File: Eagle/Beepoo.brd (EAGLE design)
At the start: 100 x 80 mm, 66 parts, among them CN1 JACK4PTH, CN2 SD-MICRO, CN3 USB-MC5F01, J1 JUMPER3-1.5MM, J2 JUMPER3-1.5MM, SW2 SLIDE1-PCM12, U1 RT9266-SOT23, U2 ATMEGA32U4, U3 AY-3-8912/28, U4 OPAMP-DUAL-SOIC8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

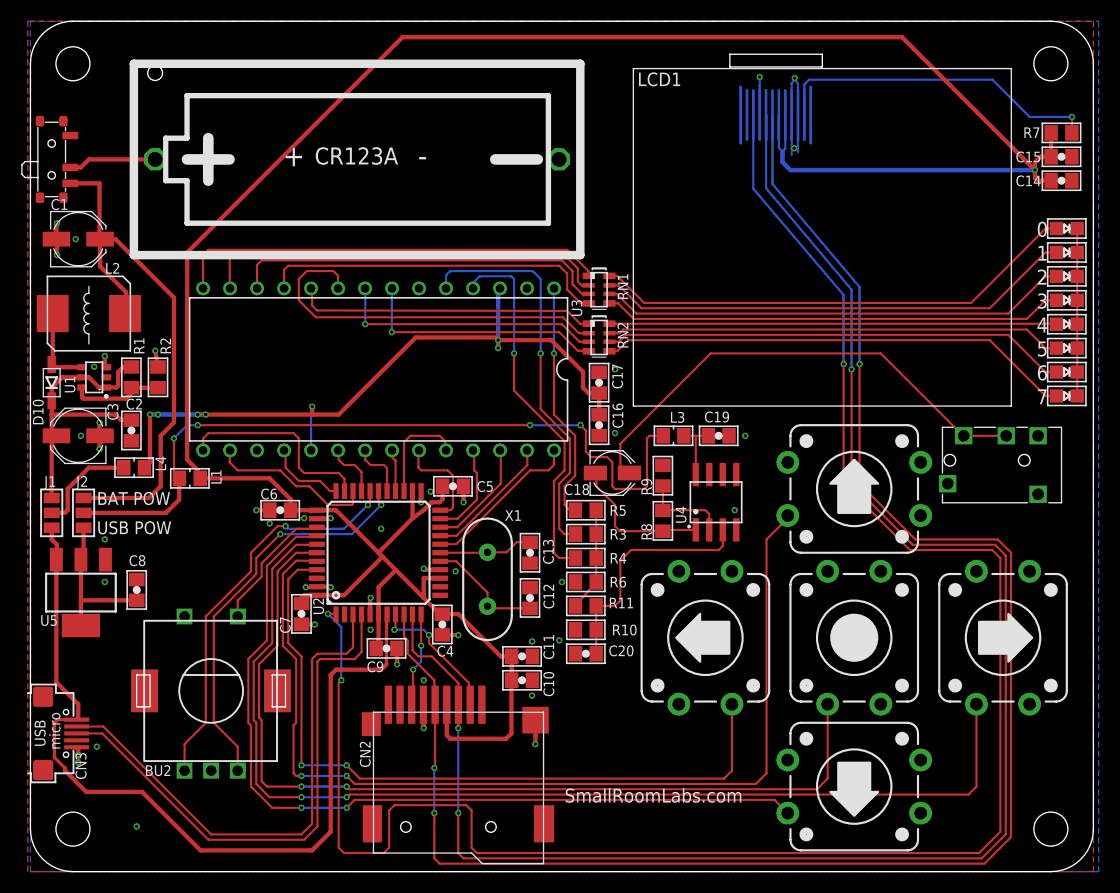
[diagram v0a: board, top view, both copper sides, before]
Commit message: Add reset to LCD. Connect A8 of AY to VCC
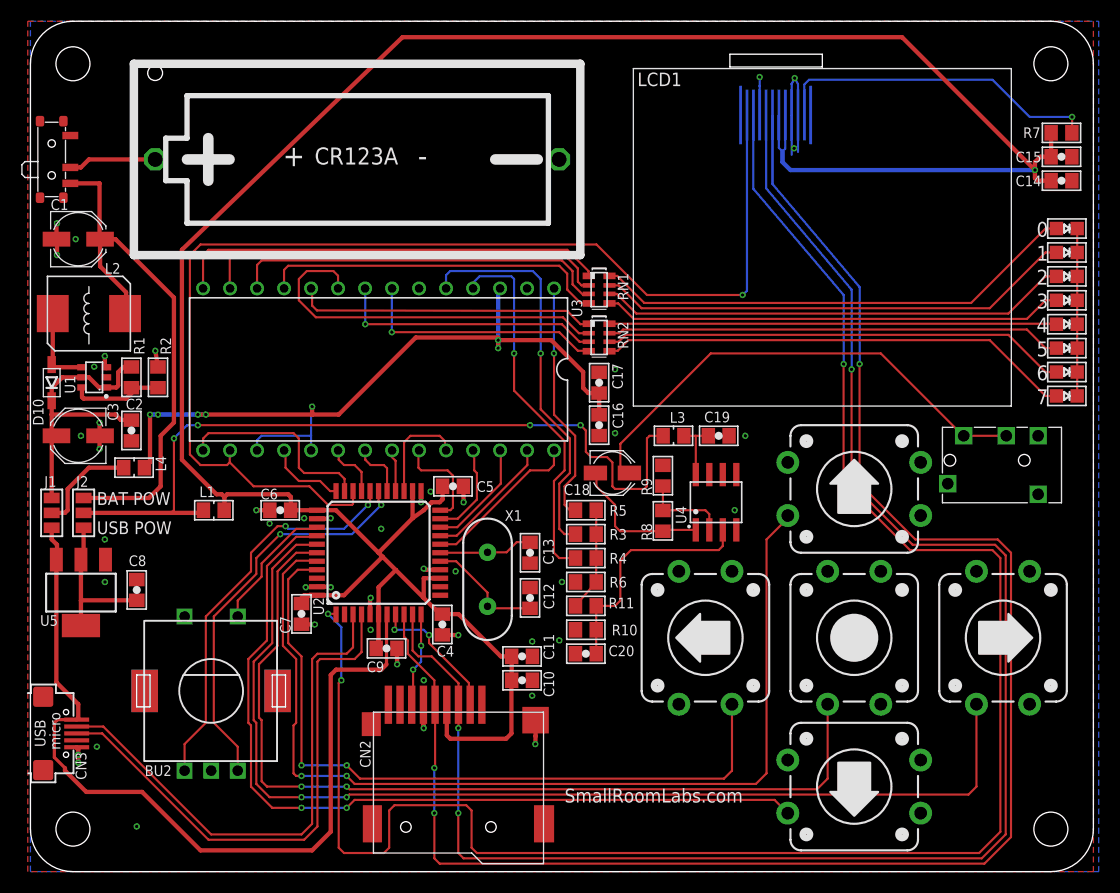
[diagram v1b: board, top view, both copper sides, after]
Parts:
- moved L1 3.75 mm to (17.2, 34.0)
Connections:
- net +5V: now also U3.17
- net AY_RESET: now also LCD1.1
- net GND: no longer U3.17
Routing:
- net AY_RESET: track 15.6 -> 110.1 mm, vias 0 -> 1
- net +5V: track 67.8 -> 74.0 mm
- net +3.3RAW: track 72.3 -> 74.7 mm
- net +3V3: track 241.0 -> 243.2 mm
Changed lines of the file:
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@@
 <?xml version="1.0" encoding="utf-8"?>
 <!DOCTYPE eagle SYSTEM "eagle.dtd">
-<eagle version="6.4">
+<eagle version="6.5.0">
 <drawing>
 <settings>
@@
 <layer number="14" name="Route14" color="1" fill="6" visible="no" active="no"/>
 <layer number="15" name="Route15" color="4" fill="6" visible="no" active="no"/>
-<layer number="16" name="Bottom" color="1" fill="1" visible="no" active="yes"/>
+<layer number="16" name="Bottom" color="1" fill="1" visible="yes" active="yes"/>
 <layer number="17" name="Pads" color="2" fill="1" visible="yes" active="yes"/>
 <layer number="18" name="Vias" color="2" fill="1" visible="yes" active="yes"/>
-<layer number="19" name="Unrouted" color="6" fill="1" visible="no" active="yes"/>
+<layer number="19" name="Unrouted" color="6" fill="1" visible="yes" active="yes"/>
 <layer number="20" name="Dimension" color="15" fill="1" visible="yes" active="yes"/>
 <layer number="21" name="tPlace" color="7" fill="1" visible="yes" active="yes"/>
@@
 <layer number="39" name="tKeepout" color="4" fill="11" visible="no" active="yes"/>
 <layer number="40" name="bKeepout" color="1" fill="11" visible="no" active="yes"/>
-<layer number="41" name="tRestrict" color="4" fill="10" visible="no" active="yes"/>
+<layer number="41" name="tRestrict" color="4" fill="10" visible="yes" active="yes"/>
 <layer number="42" name="bRestrict" color="1" fill="10" visible="no" active="yes"/>
 <layer number="43" name="vRestrict" color="2" fill="10" visible="no" active="yes"/>
@@
 <text x="95.75" y="54.375" size="1.4" layer="21" font="vector" ratio="10" rot="R180">3</text>
 <text x="95.75" y="56.625" size="1.4" layer="21" font="vector" ratio="10" rot="R180">2</text>
+<polygon width="0.2032" layer="41">
+<vertex x="53.25" y="56.5"/>
+<vertex x="54" y="56.5"/>
+<vertex x="54" y="48.5"/>
+<vertex x="53" y="48.5"/>
+<vertex x="53" y="56.5"/>
+</polygon>
 </plain>
 <attributes>
@@
 <attribute name="VALUE" x="49.0146" y="28.1364" size="1" layer="27" rot="R90"/>
 </element>
-<element name="L1" library="SRL" package="L0805" value="L-0805" x="15" y="37" smashed="yes">
-<attribute name="NAME" x="17.9808" y="36.3848" size="1" layer="25" rot="R90"/>
-<attribute name="VALUE" x="13.1364" y="34.9854" size="1" layer="27"/>
+<element name="L1" library="SRL" package="L0805" value="L-0805" x="17.25" y="34" smashed="yes">
+<attribute name="NAME" x="17.3652" y="36.2308" size="1" layer="25" rot="R180"/>
+<attribute name="VALUE" x="15.3864" y="31.9854" size="1" layer="27"/>
 </element>
 <element name="C14" library="SRL" package="C0805" value="1u" x="97" y="65" smashed="yes" rot="R180">
@@
 <via x="55" y="41.25" extent="1-16" drill="0.3048" shape="octagon"/>
 <contactref element="U3" pad="6"/>
-<contactref element="U3" pad="17"/>
 <via x="47.2" y="16.55" extent="1-16" drill="0.3048" shape="octagon"/>
 <via x="47.2" y="21.65" extent="1-16" drill="0.3048" shape="octagon"/>
@@
 <contactref element="U3" pad="3"/>
 <contactref element="U3" pad="19"/>
-<wire x1="26.4" y1="39.63" x2="26.4" y2="43.65" width="0.2032" layer="16"/>
+<wire x1="26.4" y1="39.63" x2="26.4" y2="41" width="0.2032" layer="16"/>
+<wire x1="26.4" y1="41" x2="26.4" y2="43.65" width="0.2032" layer="16"/>
 <wire x1="26.4" y1="43.65" x2="26.5" y2="43.75" width="0.2032" layer="16"/>
 <via x="26.5" y="43.75" extent="1-16" drill="0.3048" shape="octagon"/>
@@
 <wire x1="11.25" y1="43" x2="11.25" y2="38.5246" width="0.4064" layer="1"/>
 <wire x1="11.25" y1="38.5246" x2="10.7254" y2="38" width="0.4064" layer="1"/>
+<contactref element="U3" pad="17"/>
+<wire x1="21.32" y1="39.63" x2="21.32" y2="40.57" width="0.2032" layer="16"/>
+<wire x1="21.32" y1="40.57" x2="21.75" y2="41" width="0.2032" layer="16"/>
+<wire x1="21.75" y1="41" x2="26.4" y2="41" width="0.2032" layer="16"/>
 </signal>
 <signal name="AY_RESET">
@@
 <wire x1="30.25" y1="34.5" x2="28" y2="34.5" width="0.2032" layer="1"/>
 <wire x1="28" y1="34.5" x2="26.25" y2="36.25" width="0.2032" layer="1"/>
-<wire x1="26.25" y1="36.25" x2="25" y2="36.25" width="0.2032" layer="1"/>
-<wire x1="25" y1="36.25" x2="23.5" y2="37.75" width="0.2032" layer="1"/>
-<wire x1="23.5" y1="37.75" x2="19.5" y2="37.75" width="0.2032" layer="1"/>
-<wire x1="19.5" y1="37.75" x2="18.75" y2="38.5" width="0.2032" layer="1"/>
+<wire x1="26.25" y1="36.25" x2="21" y2="36.25" width="0.2032" layer="1"/>
+<wire x1="21" y1="36.25" x2="18.75" y2="38.5" width="0.2032" layer="1"/>
 <wire x1="18.75" y1="38.5" x2="18.75" y2="39.6" width="0.2032" layer="1"/>
 <wire x1="18.75" y1="39.6" x2="18.78" y2="39.63" width="0.2032" layer="1"/>
 <contactref element="U3" pad="16"/>
+<contactref element="LCD1" pad="1"/>
+<wire x1="67.41" y1="71.178" x2="67.41" y2="54.66" width="0.2032" layer="16"/>
+<wire x1="67.41" y1="54.66" x2="67" y2="54.25" width="0.2032" layer="16"/>
+<via x="67" y="54.25" extent="1-16" drill="0.3" shape="octagon"/>
+<wire x1="67" y1="54.25" x2="58" y2="54.25" width="0.2032" layer="1"/>
+<wire x1="58" y1="54.25" x2="53.25" y2="59" width="0.2032" layer="1"/>
+<wire x1="53.25" y1="59" x2="16" y2="59" width="0.2032" layer="1"/>
+<wire x1="16" y1="59" x2="15" y2="58" width="0.2032" layer="1"/>
+<wire x1="15" y1="58" x2="15" y2="39.25" width="0.2032" layer="1"/>
+<wire x1="15" y1="39.25" x2="16" y2="38.25" width="0.2032" layer="1"/>
+<wire x1="16" y1="38.25" x2="18.5" y2="38.25" width="0.2032" layer="1"/>
+<wire x1="18.5" y1="38.25" x2="18.75" y2="38.5" width="0.2032" layer="1"/>
 </signal>
 <signal name="AY_CLK">
@@
 <wire x1="94.5" y1="66" x2="82" y2="78.5" width="0.4064" layer="1"/>
 <wire x1="82" y1="78.5" x2="35" y2="78.5" width="0.4064" layer="1"/>
-<wire x1="35" y1="78.5" x2="14.75" y2="58.25" width="0.4064" layer="1"/>
+<wire x1="35" y1="78.5" x2="14.25" y2="58.5" width="0.4064" layer="1"/>
 <wire x1="70.75" y1="66.75" x2="71.5" y2="66" width="0.4064" layer="16"/>
 <wire x1="71.5" y1="66" x2="94.5" y2="66" width="0.4064" layer="16"/>
@@
 <wire x1="32.75" y1="26.75" x2="34.375" y2="28.375" width="0.4064" layer="1"/>
 <contactref element="L1" pad="2"/>
-<wire x1="14.75" y1="58.25" x2="14.75" y2="38.75" width="0.4064" layer="1"/>
-<wire x1="14.75" y1="38.75" x2="15.75" y2="37.75" width="0.4064" layer="1"/>
-<wire x1="15.75" y1="37.75" x2="15.75" y2="37.2254" width="0.4064" layer="1"/>
-<wire x1="15.75" y1="37.2254" x2="15.9754" y2="37" width="0.4064" layer="1"/>
-<wire x1="15.9754" y1="37" x2="22.5" y2="37" width="0.4064" layer="1"/>
-<wire x1="22.5" y1="37" x2="24.5" y2="35" width="0.4064" layer="1"/>
-<wire x1="24.5" y1="35" x2="24.5" y2="34.0246" width="0.4064" layer="1"/>
+<wire x1="14.25" y1="58.5" x2="14.25" y2="38.75" width="0.4064" layer="1"/>
 <wire x1="24.5" y1="34.0246" x2="24.4754" y2="34" width="0.4064" layer="1"/>
+<wire x1="24.5" y1="34.0246" x2="24.5" y2="35.25" width="0.4064" layer="1"/>
+<wire x1="24.5" y1="35.25" x2="24.25" y2="35.5" width="0.4064" layer="1"/>
+<wire x1="24.25" y1="35.5" x2="18.5" y2="35.5" width="0.4064" layer="1"/>
+<wire x1="18.5" y1="35.5" x2="18.25" y2="35.25" width="0.4064" layer="1"/>
+<wire x1="18.25" y1="35.25" x2="18.25" y2="34.0246" width="0.4064" layer="1"/>
+<wire x1="18.25" y1="34.0246" x2="18.2254" y2="34" width="0.4064" layer="1"/>
+<wire x1="14.25" y1="38.75" x2="17.5" y2="35.5" width="0.4064" layer="1"/>
+<wire x1="17.5" y1="35.5" x2="18" y2="35.5" width="0.4064" layer="1"/>
+<wire x1="18" y1="35.5" x2="18.25" y2="35.25" width="0.4064" layer="1"/>
 </signal>
 <signal name="BAT-SWITCHED">
@@
 <wire x1="14.75" y1="42" x2="13.5" y2="40.75" width="0.2032" layer="16"/>
 <via x="13.5" y="40.75" extent="1-16" drill="0.3048" shape="octagon"/>
-<wire x1="13.5" y1="40.75" x2="13.5" y2="36.7746" width="0.2032" layer="1"/>
-<wire x1="5" y1="33.75" x2="12.75" y2="33.75" width="0.4064" layer="1"/>
-<wire x1="12.75" y1="33.75" x2="14" y2="35" width="0.4064" layer="1"/>
-<wire x1="14" y1="35" x2="14" y2="36.2254" width="0.4064" layer="1"/>
-<wire x1="14" y1="36.2254" x2="14.0246" y2="37" width="0.4064" layer="1"/>
-<wire x1="13.5" y1="36.7746" x2="14.0246" y2="37" width="0.2032" layer="1"/>
+<wire x1="13.5" y1="40.75" x2="13.5" y2="34" width="0.2032" layer="1"/>
+<wire x1="5" y1="33.75" x2="13.25" y2="33.75" width="0.4064" layer="1"/>
+<wire x1="13.25" y1="33.75" x2="16.0246" y2="33.75" width="0.4064" layer="1"/>
+<wire x1="16.0246" y1="33.75" x2="16.2746" y2="34" width="0.4064" layer="1"/>
+<wire x1="13.5" y1="34" x2="13.25" y2="33.75" width="0.2032" layer="1"/>
 </signal>
 <signal name="N$15">
